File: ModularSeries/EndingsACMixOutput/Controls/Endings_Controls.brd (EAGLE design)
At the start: 48.5 x 100 mm, 14 parts

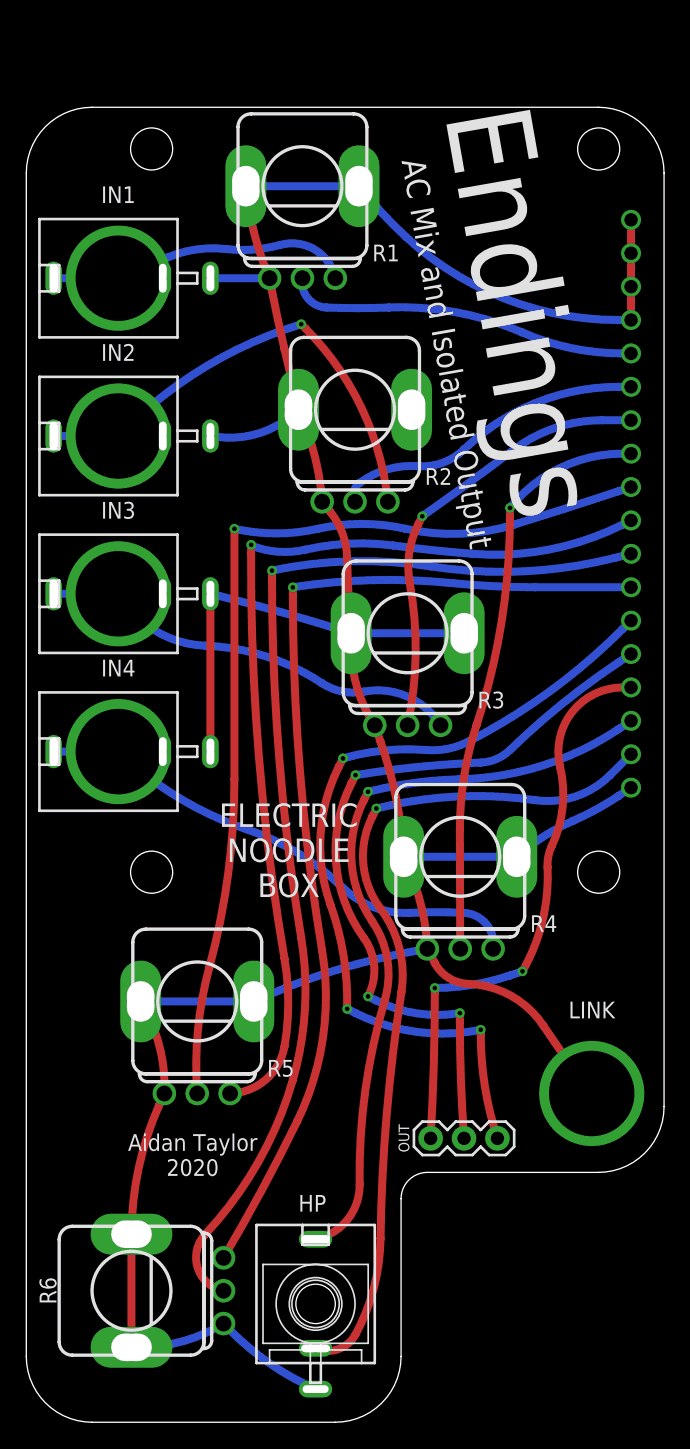
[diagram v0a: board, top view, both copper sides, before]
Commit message: Endings panel added
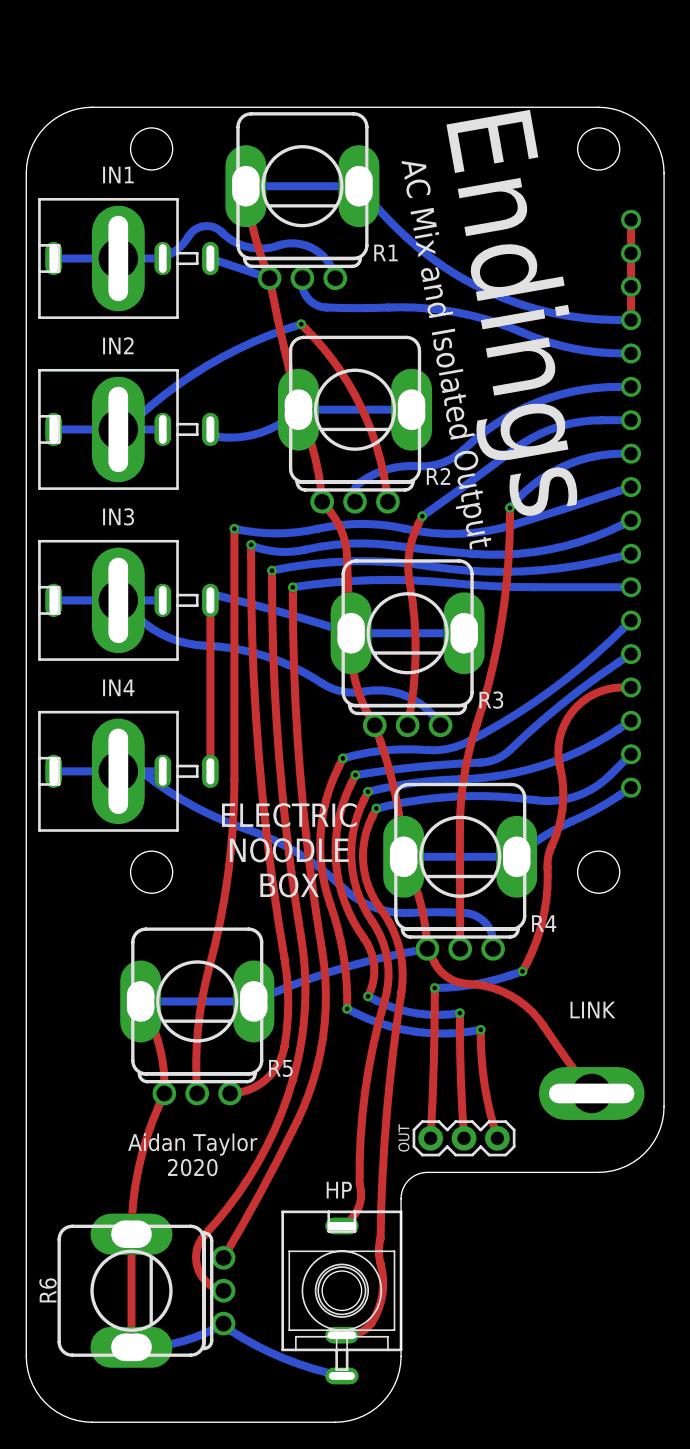
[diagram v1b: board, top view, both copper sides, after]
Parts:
- IN1, IN2, IN3, IN4: value COMBI-JACK -> COMBI-JACKCINCHNANA; device ElectricNoodleBox:COMBOJACK_PANEL -> ElectricNoodleBox:NEWCOMBOJACK_PANEL
- LINK: device ElectricNoodleBox:BANANA_PANEL -> ElectricNoodleBox:CINCHNANA_PANEL
- moved HP 2.24 mm to (25.0, 10.0)
- moved IN1 1.50 mm to (8.00, 88.5)
- moved IN4 1.50 mm to (8.00, 49.5)
- moved IN2 0.50 mm to (8.00, 75.5)
- moved IN3 0.50 mm to (8.00, 62.5)
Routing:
- net AGND: track 244.7 -> 256.2 mm
- net N$1: track 25.9 -> 22.9 mm
- net N$17: track 56.3 -> 54.4 mm
- net N$16: track 64.2 -> 62.4 mm

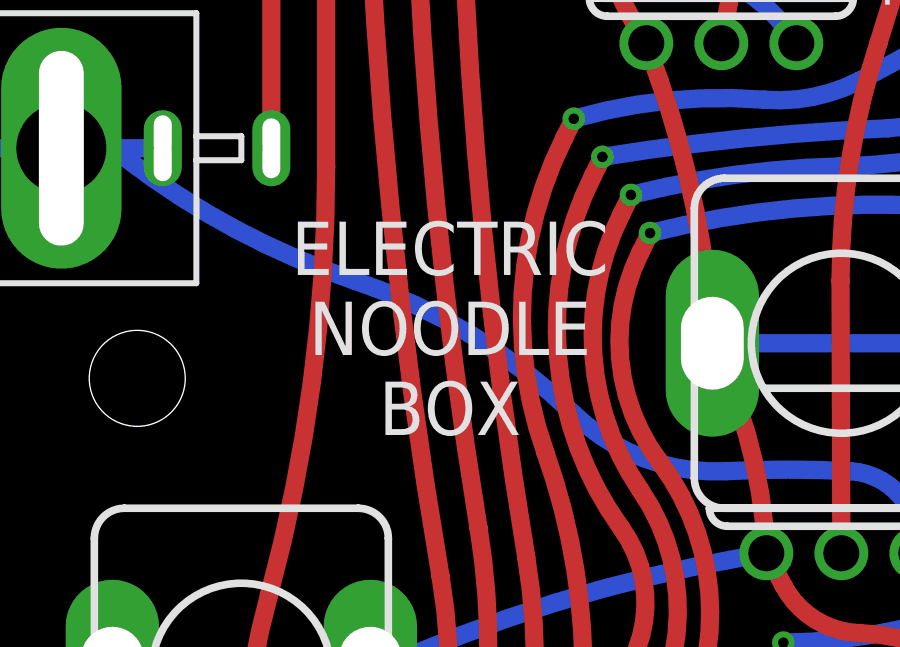
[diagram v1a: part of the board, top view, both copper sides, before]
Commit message: Panel for TimeSeeds added. TLHP core PCB added
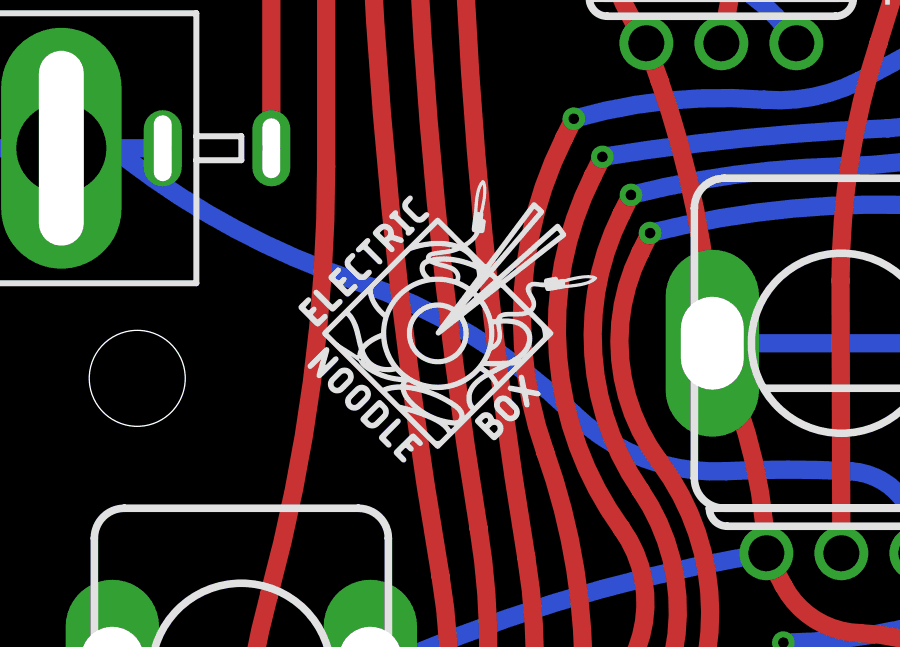
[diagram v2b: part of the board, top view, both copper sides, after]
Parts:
- added U$1, U$2: (no value), ElectricNoodleBox:LOGO10X10
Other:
- board text removed: "ELECTRIC NOODLE BOX"
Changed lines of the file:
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@@
 <?xml version="1.0" encoding="utf-8"?>
 <!DOCTYPE eagle SYSTEM "eagle.dtd">
-<eagle version="9.6.0">
+<eagle version="9.6.2">
 <drawing>
 <settings>
@@
 <layer number="47" name="Measures" color="7" fill="1" visible="no" active="yes"/>
 <layer number="48" name="Document" color="7" fill="1" visible="yes" active="yes"/>
-<layer number="49" name="Reference" color="7" fill="1" visible="yes" active="yes"/>
+<layer number="49" name="Reference" color="7" fill="1" visible="no" active="yes"/>
 <layer number="50" name="dxf" color="7" fill="1" visible="no" active="no"/>
 <layer number="51" name="tDocu" color="7" fill="1" visible="yes" active="yes"/>
@@
 </layers>
 <board>
+<fusionsync huburn="a.cGVyc29uYWw6dWUyYjdlNGE0" projecturn="a.cGVyc29uYWw6dWUyYjdlNGE0IzIwMjAwNDA1MjgzMzA0MTgx" f3durn="urn:adsk.wipprod:dm.lineage:C9mXlbdfSfOkebZVyaMQkw" pcbguid="ca77d775-e66d-4b84-9e6c-b0223febc801" lastpulledtime="" lastsyncedchangeguid="" latestrevisionid="103a2d42-0e34-4fa8-aada-3ce8ce754bf7" lastsyncedrevisionid="103a2d42-0e34-4fa8-aada-3ce8ce754bf7" lastboardhashguid="a0248c47-75f6-c8d9-bd6f-9e9e8582f66e" lastpushedtime="2020-06-25T11:20:22Z" linktopcb3d="true"/>
 <plain>
 <wire x1="0" y1="-14.25" x2="50.5" y2="-14.25" width="0.1524" layer="49"/>
@@
 <text x="38.735" y="84.455" size="6.4516" layer="21" font="vector" ratio="16" rot="R280" align="center">Endings</text>
 <text x="33.02" y="81.28" size="1.778" layer="21" font="vector" ratio="16" rot="R280" align="center">AC Mix and Isolated Output</text>
-<text x="20.955" y="43.4975" size="1.778" layer="21" font="vector" ratio="16" align="center">ELECTRIC
-NOODLE
-BOX</text>
 <text x="13.6525" y="20.32" size="1.27" layer="21" font="vector" ratio="16" align="center">Aidan Taylor
 2020</text>
@@
 <attribute name="NAME" x="8" y="55.85" size="1.27" layer="25" font="vector" rot="R180" align="center"/>
 </element>
+<element name="U$1" library="ElectricNoodleBox" package="LOGO10X10" value="" x="15.875" y="38.735" smashed="yes"/>
+<element name="U$2" library="ElectricNoodleBox" package="LOGO10X10" value="" x="25.7175" y="38.4175" smashed="yes" rot="MR0"/>
 </elements>
 <signals>
@@
 which will not be processed correctly with this version.
 </note>
+<note version="8.3" severity="warning">
+Since Version 8.3, EAGLE supports Fusion synchronisation.
+This feature will not be available in this version and saving
+the document will break the link to the Fusion PCB feature.
+</note>
 </compatibility>

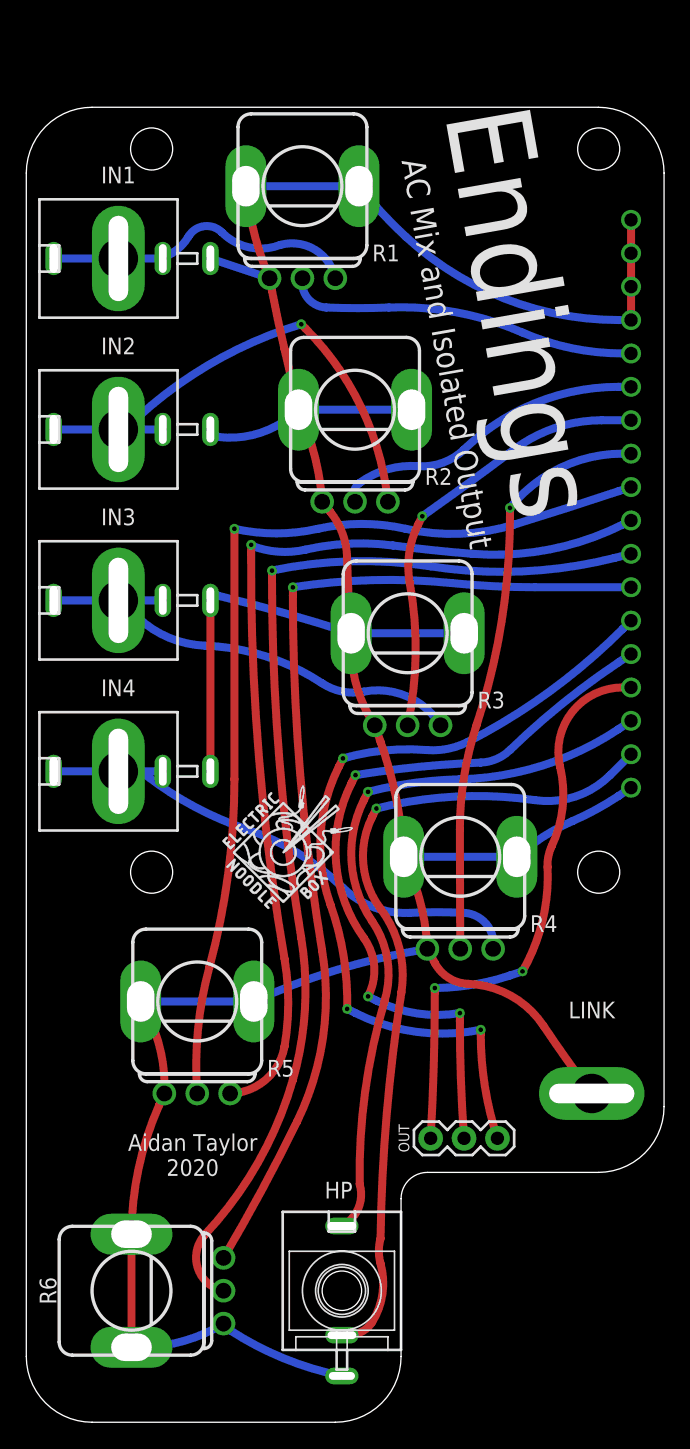
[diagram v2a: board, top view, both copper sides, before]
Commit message: Layout and schematic renders for LHP added
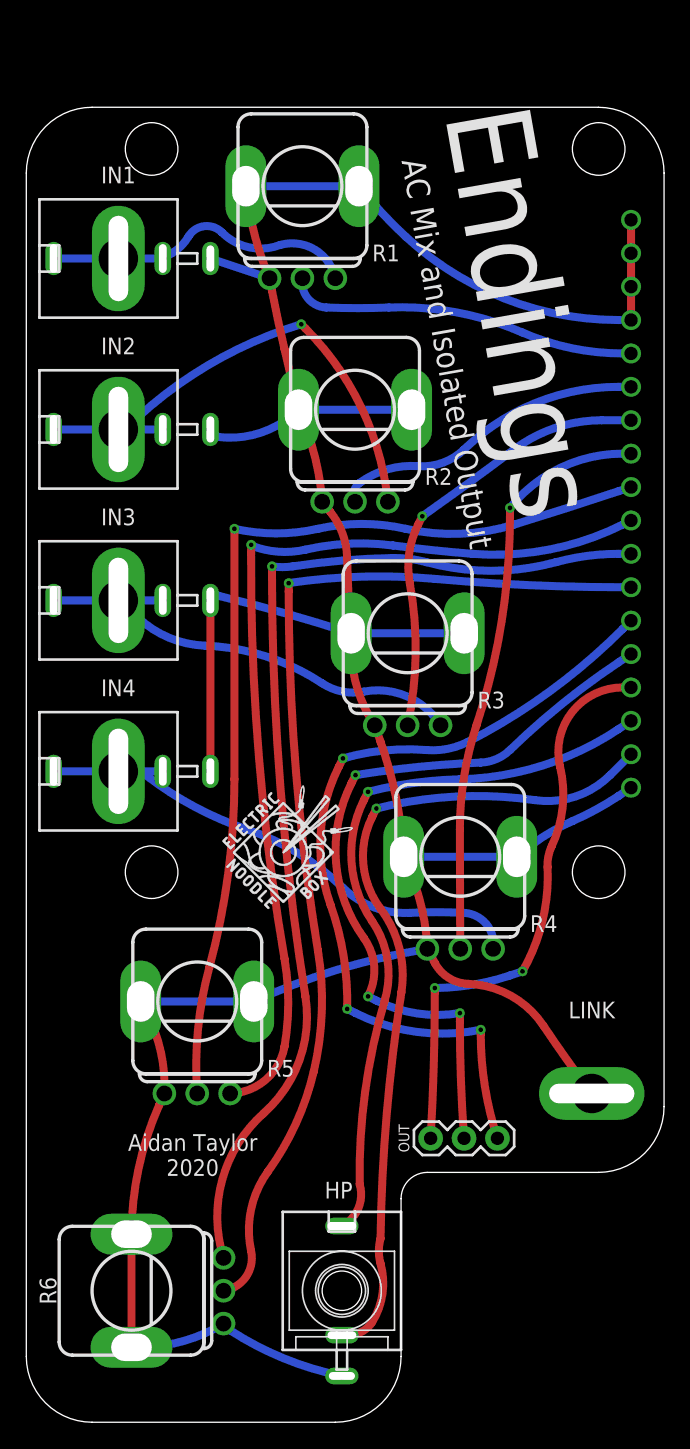
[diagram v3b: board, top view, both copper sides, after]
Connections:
- net N$10: now also BOARD1.MSTRVOLIN; no longer BOARD1.MSTR2
- net N$11: now also BOARD1.HPVOLIN; no longer BOARD1.HPV3
- net N$12: now also BOARD1.HPVOLOUT; no longer BOARD1.HPV2
- net N$9: now also BOARD1.MSTRVOLOUT; no longer BOARD1.MSTR3
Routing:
- net N$12: track 84.2 -> 81.5 mm
- net N$11: track 78.4 -> 81.0 mm
- net AGND: track 256.2 -> 255.4 mm
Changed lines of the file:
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@@
 </layers>
 <board>
-<fusionsync huburn="a.cGVyc29uYWw6dWUyYjdlNGE0" projecturn="a.cGVyc29uYWw6dWUyYjdlNGE0IzIwMjAwNDA1MjgzMzA0MTgx" f3durn="urn:adsk.wipprod:dm.lineage:C9mXlbdfSfOkebZVyaMQkw" pcbguid="ca77d775-e66d-4b84-9e6c-b0223febc801" lastpulledtime="" lastsyncedchangeguid="" latestrevisionid="103a2d42-0e34-4fa8-aada-3ce8ce754bf7" lastsyncedrevisionid="103a2d42-0e34-4fa8-aada-3ce8ce754bf7" lastboardhashguid="a0248c47-75f6-c8d9-bd6f-9e9e8582f66e" lastpushedtime="2020-06-25T11:20:22Z" linktopcb3d="true"/>
+<fusionsync huburn="a.cGVyc29uYWw6dWUyYjdlNGE0" projecturn="a.cGVyc29uYWw6dWUyYjdlNGE0IzIwMjAwNDA1MjgzMzA0MTgx" f3durn="urn:adsk.wipprod:dm.lineage:C9mXlbdfSfOkebZVyaMQkw" pcbguid="" lastpulledtime="" lastsyncedchangeguid="" latestrevisionid="103a2d42-0e34-4fa8-aada-3ce8ce754bf7" lastsyncedrevisionid="103a2d42-0e34-4fa8-aada-3ce8ce754bf7" lastboardhashguid="a0248c47-75f6-c8d9-bd6f-9e9e8582f66e" lastpushedtime="2020-06-25T11:20:22Z" linktopcb3d="true"/>
 <plain>
 <wire x1="0" y1="-14.25" x2="50.5" y2="-14.25" width="0.1524" layer="49"/>
@@
 <wire x1="15" y1="62.5" x2="15" y2="49.5" width="0.6096" layer="1"/>
 <wire x1="29.7" y1="43" x2="38.3" y2="43" width="0.6096" layer="16"/>
-<wire x1="38.3" y1="43" x2="38.4175" y2="42.2275" width="0.6096" layer="1"/>
 <contactref element="BOARD1" pad="HPOUTS"/>
 <contactref element="HP" pad="S"/>
@@
 </signal>
 <signal name="N$9">
-<contactref element="BOARD1" pad="MSTR3"/>
+<contactref element="BOARD1" pad="MSTRVOLOUT"/>
 <contactref element="R5" pad="C3"/>
 <wire x1="46.99" y1="68.58" x2="46.355" y2="68.2625" width="0.6096" layer="16"/>
@@
 <signal name="N$10">
 <contactref element="R5" pad="C2"/>
-<contactref element="BOARD1" pad="MSTR2"/>
+<contactref element="BOARD1" pad="MSTRVOLIN"/>
 <wire x1="46.99" y1="71.12" x2="46.0375" y2="70.8025" width="0.6096" layer="16"/>
 <wire x1="46.0375" y1="70.8025" x2="38.1" y2="68.2625" width="0.6096" layer="16" curve="-1.380554"/>
@@
 <wire x1="14.9225" y1="34.6075" x2="14" y2="25" width="0.6096" layer="1" curve="19.409281"/>
 <wire x1="16.8275" y1="67.945" x2="16.8275" y2="48.895" width="0.6096" layer="1"/>
-</signal>
-<signal name="N$11">
-<contactref element="BOARD1" pad="HPV3"/>
-<contactref element="R6" pad="C3"/>
-<wire x1="39.6875" y1="63.5" x2="33.3375" y2="63.8175" width="0.6096" layer="16" curve="-5.72481"/>
-<wire x1="33.3375" y1="63.8175" x2="21.2725" y2="63.5" width="0.6096" layer="16" curve="14.464541"/>
-<wire x1="21.2725" y1="63.5" x2="21.27271875" y2="63.49165" width="0.6096" layer="16" curve="165.497681"/>
-<via x="21.27271875" y="63.49165" extent="1-16" drill="0.35"/>
-<wire x1="21.27271875" y1="63.49165" x2="21.2725" y2="62.865" width="0.6096" layer="1"/>
-<wire x1="21.2725" y1="62.865" x2="23.495" y2="35.8775" width="0.6096" layer="1" curve="9.455706"/>
-<wire x1="23.495" y1="35.8775" x2="21.59" y2="22.86" width="0.6096" layer="1" curve="-35.522746"/>
-<wire x1="21.59" y1="22.86" x2="16" y2="12.5" width="0.6096" layer="1" curve="-4.526325"/>
-<wire x1="46.99" y1="63.5" x2="39.6875" y2="63.5" width="0.6096" layer="16"/>
-</signal>
-<signal name="N$12">
-<contactref element="R6" pad="C2"/>
-<contactref element="BOARD1" pad="HPV2"/>
-<wire x1="46.99" y1="66.04" x2="45.72" y2="65.7225" width="0.6096" layer="16"/>
-<wire x1="45.72" y1="65.7225" x2="31.75" y2="65.0875" width="0.6096" layer="16" curve="-22.867363"/>
-<wire x1="31.75" y1="65.0875" x2="19.685" y2="64.77" width="0.6096" layer="16" curve="20.677163"/>
-<wire x1="19.685" y1="64.77" x2="19.68521875" y2="64.76165" width="0.6096" layer="16" curve="159.300595"/>
-<via x="19.68521875" y="64.76165" extent="1-16" drill="0.35"/>
-<wire x1="19.68521875" y1="64.76165" x2="19.685" y2="64.135" width="0.6096" layer="1"/>
-<wire x1="19.685" y1="64.135" x2="21.9075" y2="36.83" width="0.6096" layer="1" curve="9.346705"/>
-<wire x1="21.9075" y1="36.83" x2="21.2725" y2="26.035" width="0.6096" layer="1" curve="-25.386363"/>
-<wire x1="21.2725" y1="26.035" x2="14.605" y2="14.2875" width="0.6096" layer="1" curve="-27.036366"/>
-<wire x1="14.605" y1="14.2875" x2="16" y2="10" width="0.6096" layer="1" curve="122.238086"/>
 </signal>
 <signal name="N$13">
@@
 <wire x1="33.9725" y1="30.48" x2="34.29" y2="21.59" width="0.6096" layer="1" curve="4.090817"/>
 </signal>
+<signal name="N$11">
+<contactref element="BOARD1" pad="HPVOLIN"/>
+<contactref element="R6" pad="C3"/>
+<wire x1="46.99" y1="66.04" x2="46.0375" y2="66.04" width="0.6096" layer="16"/>
+<wire x1="46.0375" y1="66.04" x2="41.275" y2="65.405" width="0.6096" layer="16" curve="15.189287"/>
+<wire x1="41.275" y1="65.405" x2="31.4325" y2="65.405" width="0.6096" layer="16" curve="-30.37859"/>
+<wire x1="31.4325" y1="65.405" x2="28.8925" y2="65.7225" width="0.6096" layer="16" curve="16.128583"/>
+<wire x1="28.8925" y1="65.7225" x2="21.2725" y2="65.0875" width="0.6096" layer="16" curve="7.648701"/>
+<wire x1="21.2725" y1="65.0875" x2="19.685" y2="65.0875" width="0.6096" layer="16" curve="-17.175961"/>
+<via x="19.685" y="65.0875" extent="1-16" drill="0.35"/>
+<wire x1="19.685" y1="65.0875" x2="19.685" y2="64.4525" width="0.6096" layer="1"/>
+<wire x1="19.685" y1="64.4525" x2="22.225" y2="32.385" width="0.6096" layer="1" curve="9.057648"/>
+<wire x1="22.225" y1="32.385" x2="19.05" y2="23.495" width="0.6096" layer="1" curve="-57.422932"/>
+<wire x1="19.05" y1="23.495" x2="16" y2="12.5" width="0.6096" layer="1" curve="65.722711"/>
+</signal>
+<signal name="N$12">
+<contactref element="R6" pad="C2"/>
+<contactref element="BOARD1" pad="HPVOLOUT"/>
+<wire x1="46.99" y1="63.5" x2="46.355" y2="63.5" width="0.6096" layer="16"/>
+<wire x1="46.355" y1="63.5" x2="32.0675" y2="64.135" width="0.6096" layer="16" curve="-5.089609"/>
+<wire x1="32.0675" y1="64.135" x2="20.955" y2="63.8175" width="0.6096" layer="16" curve="13.452413"/>
+<wire x1="20.955" y1="63.8175" x2="20.955259375" y2="63.8084375" width="0.6096" layer="16" curve="166.586936"/>
+<via x="20.955259375" y="63.8084375" extent="1-16" drill="0.35"/>
+<wire x1="20.955259375" y1="63.8084375" x2="20.955" y2="63.1825" width="0.6096" layer="1"/>
+<wire x1="20.955" y1="63.1825" x2="23.1775" y2="35.8775" width="0.6096" layer="1" curve="9.354188"/>
+<wire x1="23.1775" y1="35.8775" x2="22.86" y2="26.67" width="0.6096" layer="1" curve="-22.610732"/>
+<wire x1="22.86" y1="26.67" x2="19.3675" y2="19.05" width="0.6096" layer="1" curve="-22.686545"/>
+<wire x1="19.3675" y1="19.05" x2="18.0975" y2="13.0175" width="0.6096" layer="1" curve="48.15638"/>
+<wire x1="18.0975" y1="13.0175" x2="16" y2="10" width="0.6096" layer="1" curve="-93.986323"/>
+</signal>
 </signals>
